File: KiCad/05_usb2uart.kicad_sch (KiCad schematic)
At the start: 16 parts, among them IC501 FT232RL-REEL, J301 USB_C_Receptacle_USB2.0, U301 USBLC6-2SC6

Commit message: First scheme complete
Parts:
- removed D301, D302: LED, LED_SMD:LED_0603_1608Metric, symbol Device:LED
- removed R301, R302: 0R, Resistor_SMD:R_0805_2012Metric, symbol Device:R
- removed R305, R306: 510R, Resistor_SMD:R_0402_1005Metric, symbol Device:R
- added C503: 22uF, Capacitor_SMD:C_0805_2012Metric, symbol Device:C
- added D501, D502, D503: LED, LED_SMD:LED_0603_1608Metric, symbol Device:LED
- added J501, J502: Conn_01x09_Pin, Connector_PinHeader_2.54mm:PinHeader_1x09_P2.54mm_Vertical, symbol Connector:Conn_01x09_Pin
- added J503: Conn_01x06_Pin, Connector_PinHeader_2.54mm:PinHeader_1x06_P2.54mm_Vertical, symbol Connector:Conn_01x06_Pin
- added R503, R504, R505: 510R, Resistor_SMD:R_0402_1005Metric, symbol Device:R
- renumbered C502 to C501, C501 to C502, C304 to C504, C305 to C505, J301 to J504, R303 to R501, R304 to R502, R307 to R506, U301 to U501
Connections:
- net +VCC_USB2UART_FILT: now also D501.2 (A), D502.2 (A), J502.6 (Pin_6)
- net GND: now also C503.2, D503.1 (K), J501.7 (Pin_7), J502.8 (Pin_8), J503.6 (Pin_6)
- net RXD: now also IC501.5 (RXD), J501.5 (Pin_5), J503.2 (Pin_2)
- net RX_LED: now also R504.1
- net TXD: now also IC501.1 (TXD), J501.1 (Pin_1), J503.3 (Pin_3)
- net TX_LED: now also J502.7 (Pin_7), R505.1
- net DCD: now reaches IC501.10 (DCD#)
- net DCD: now also J501.8 (Pin_8), J501.9 (Pin_9)
- net CTS: now reaches IC501.11 (CTS#)
- net CTS: now also J502.4 (Pin_4), J503.5 (Pin_5)
- net SLEEP: now reaches IC501.12 (CBUS4)
- net SLEEP: now also J502.3 (Pin_3)
- net TEN: now reaches IC501.13 (CBUS2)
- net TEN: now also J502.2 (Pin_2)
- net PWREN: now reaches IC501.14 (CBUS3)
- net PWREN: now also J502.1 (Pin_1)
- net +3V3_FTDI: now reaches IC501.17 (3V3OUT)
- net +3V3_FTDI: now also C503.1, J502.5 (Pin_5), R503.2
- net DTR: now reaches IC501.2 (DTR#)
- net DTR: now also J501.2 (Pin_2), J502.9 (Pin_9), J503.1 (Pin_1)
- net RTS: now reaches IC501.3 (RTS#)
- net RTS: now also J501.3 (Pin_3)
- net RI: now reaches IC501.6 (RI#)
- net RI: now also J501.6 (Pin_6)
- net DSR: now reaches IC501.9 (DSR#)
- new net: D501.1 (K), R504.2
- new net: D503.2 (A), R503.1
- new net: D502.1 (K), R505.2
- new net FTDI_VCC: J503.4 (Pin_4)
- new net VCC_FTDI: J501.4 (Pin_4)
- no-connect marks 9 -> 5
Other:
- note added: "Pin headers"
- note added: "Power indication"
- note added: "TX/RX indication"
- moved on the sheet: C501, C502, C504, IC501, J504, R501, R502, U501

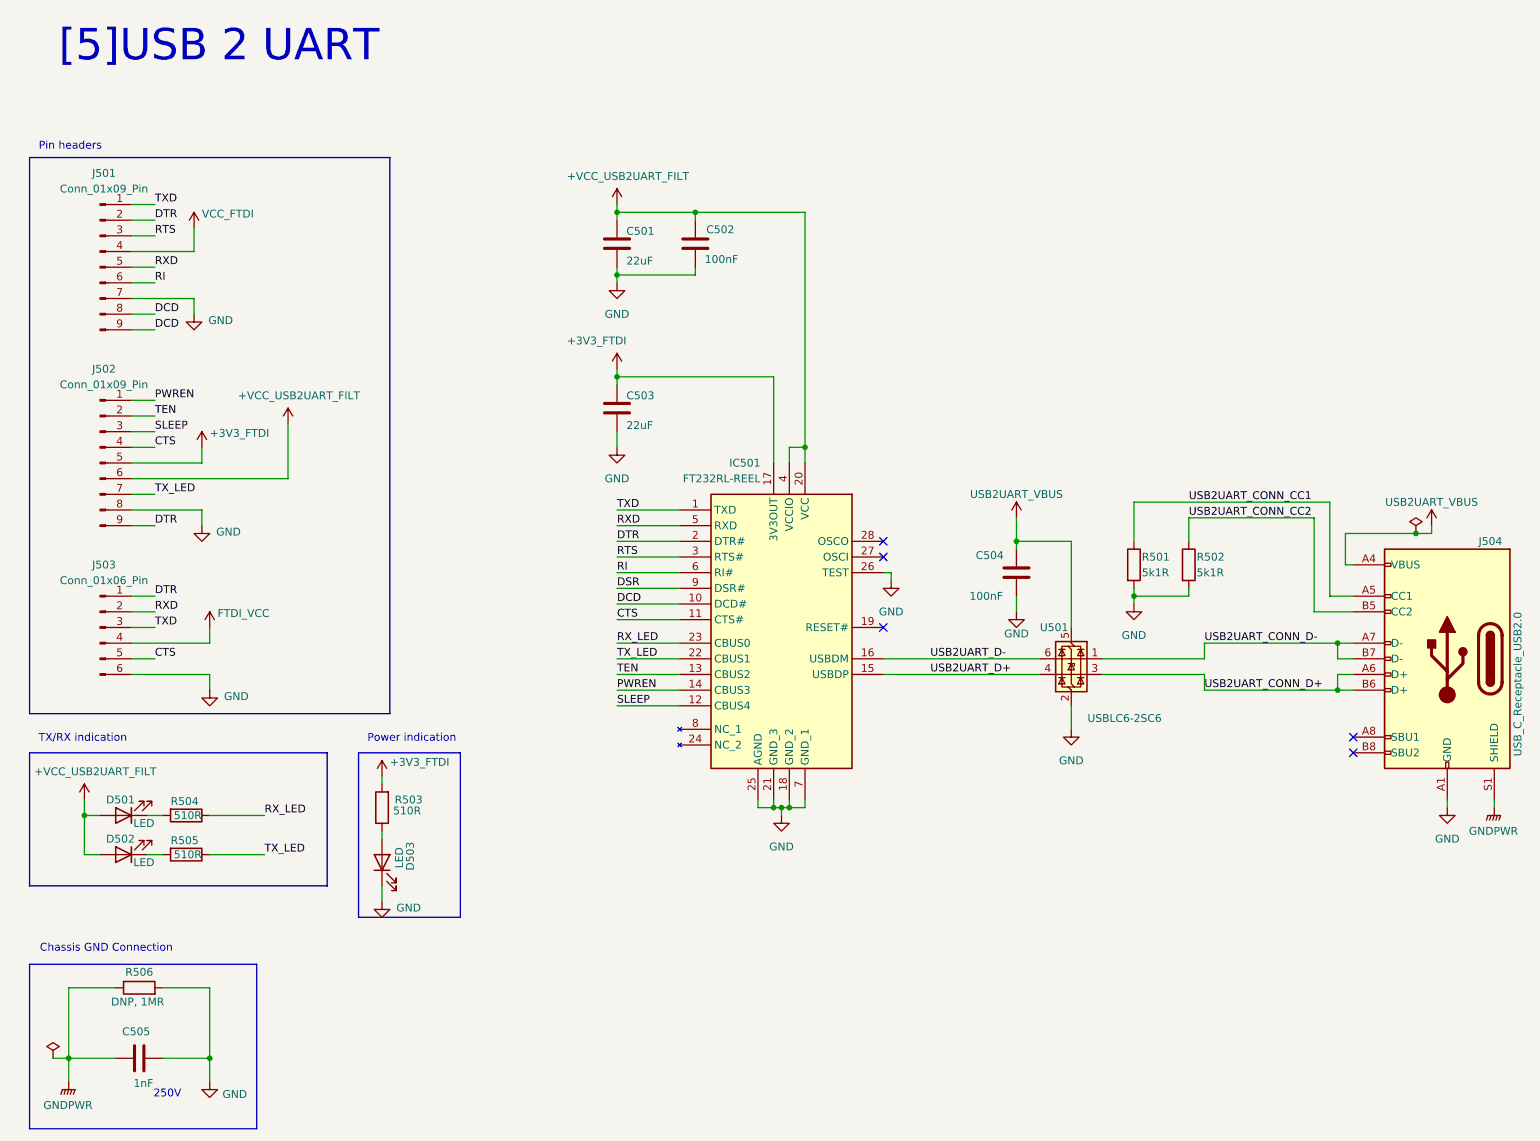
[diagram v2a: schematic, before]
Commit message: ERC fixes
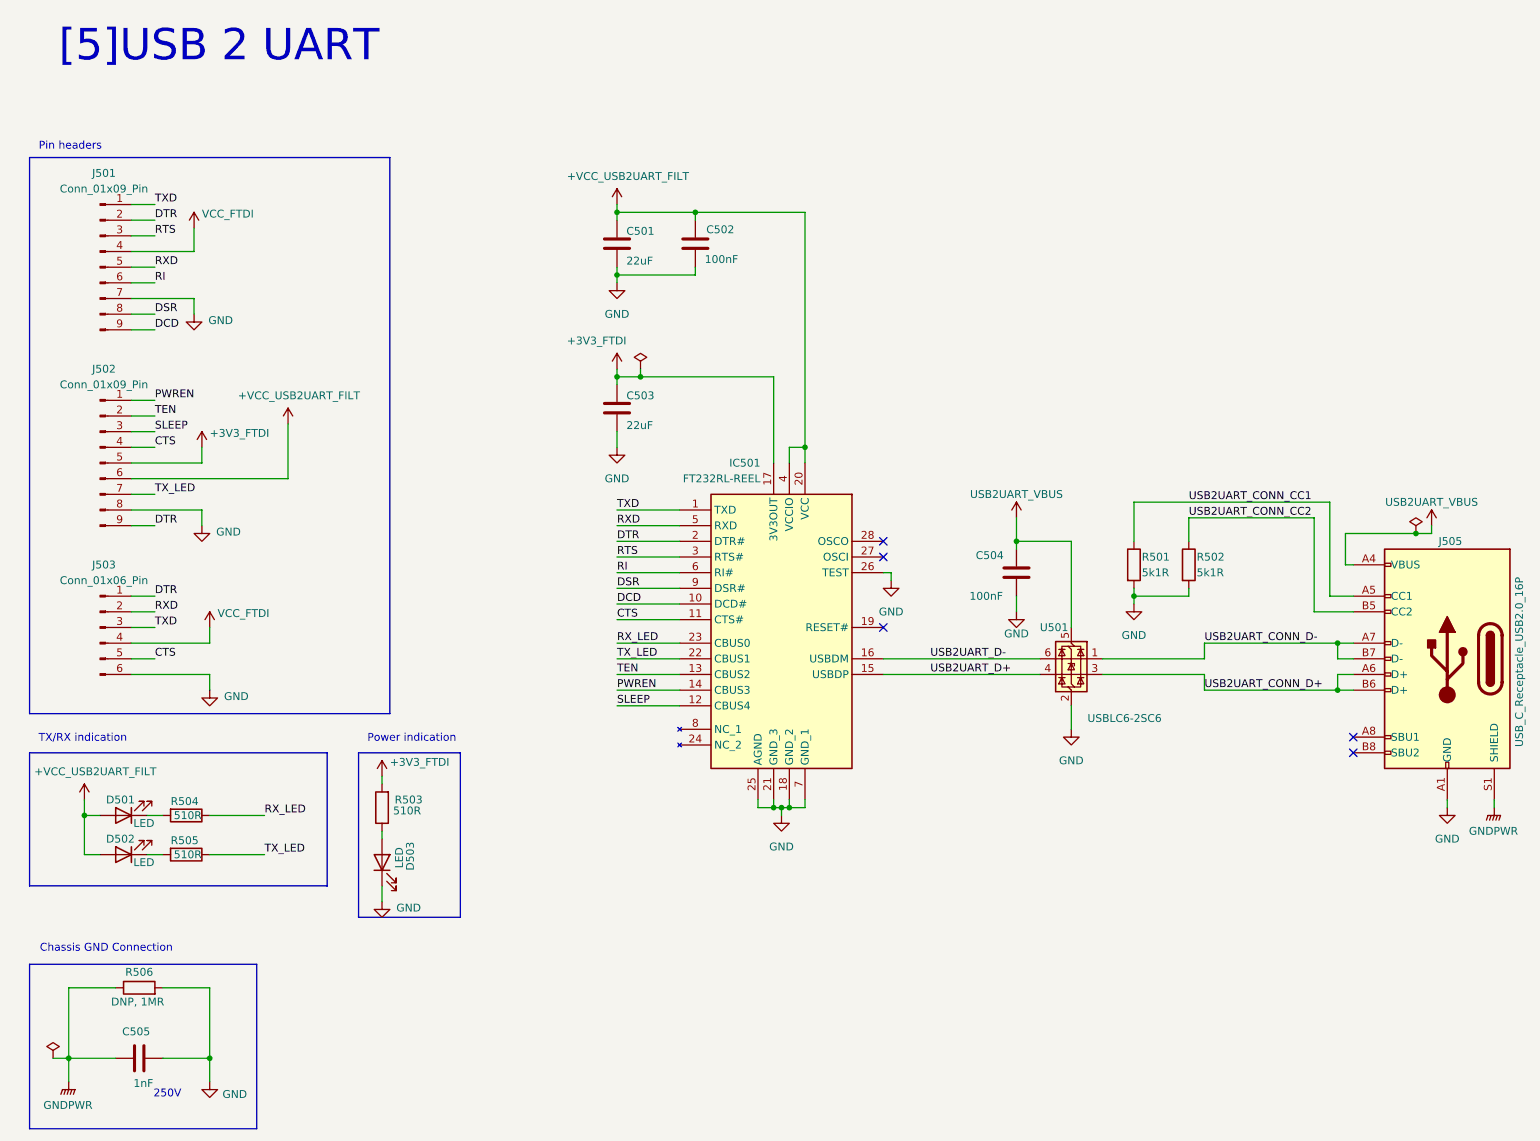
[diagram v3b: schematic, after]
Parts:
- removed J504: USB_C_Receptacle_USB2.0, Connector_USB:USB_C_Receptacle_HRO_TYPE-C-31-M-12, symbol Connector:USB_C_Receptacle_USB2.0
- added J505: USB_C_Receptacle_USB2.0_16P, Connector_USB:USB_C_Receptacle_HRO_TYPE-C-31-M-12, symbol Connector:USB_C_Receptacle_USB2.0_16P
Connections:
- net FTDI_VCC is gone; now on net VCC_FTDI: J503.4 (Pin_4)
- net DCD: no longer J501.8 (Pin_8)
- net DSR: now also J501.8 (Pin_8)
- net GND: now also J505.A1 (GND), J505.A12 (GND), J505.B1 (GND), J505.B12 (GND)
- net GNDPWR: now also J505.S1 (SHIELD)
- net USB2UART_CONN_CC1: now also J505.A5 (CC1)
- net USB2UART_CONN_CC2: now also J505.B5 (CC2)
- net USB2UART_CONN_D+: now also J505.A6 (D+), J505.B6 (D+)
- net USB2UART_CONN_D-: now also J505.A7 (D-), J505.B7 (D-)
- net USB2UART_VBUS: now also J505.A4 (VBUS), J505.A9 (VBUS), J505.B4 (VBUS), J505.B9 (VBUS)

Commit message: basic PCB
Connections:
- net DTR: no longer J502.9 (Pin_9)
- net RX_LED: now also J502.9 (Pin_9)
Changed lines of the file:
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@@
+		)
+	)
+	(label "RX_LED"
+		(at 34.29 97.79 0)
+		(effects
+			(font
+				(size 1.27 1.27)
+			)
+			(justify left bottom)
 		)
 	)
@@
 		)
 	)
-	(label "DTR"
-		(at 34.29 97.79 0)
-		(effects
-			(font
-				(size 1.27 1.27)
-			)
-			(justify left bottom)
-		)
-	)
 	(label "TEN"
 		(at 109.22 121.92 0)
@@
 		(dnp no)
 		(property "Reference" "R503"
-			(at 75.438 142.24 0)
+			(at 74.93 141.986 0)
 			(effects
 				(font
@@
 		(dnp no)
 		(property "Reference" "D503"
-			(at 75.692 151.384 0)
+			(at 75.692 151.384 90)
 			(effects
 				(font
@@
 		)
 		(property "Value" "LED"
-			(at 73.914 151.638 0)
-			(effects
-				(font
+			(at 75.692 153.162 90)
+			(effects
+				(font

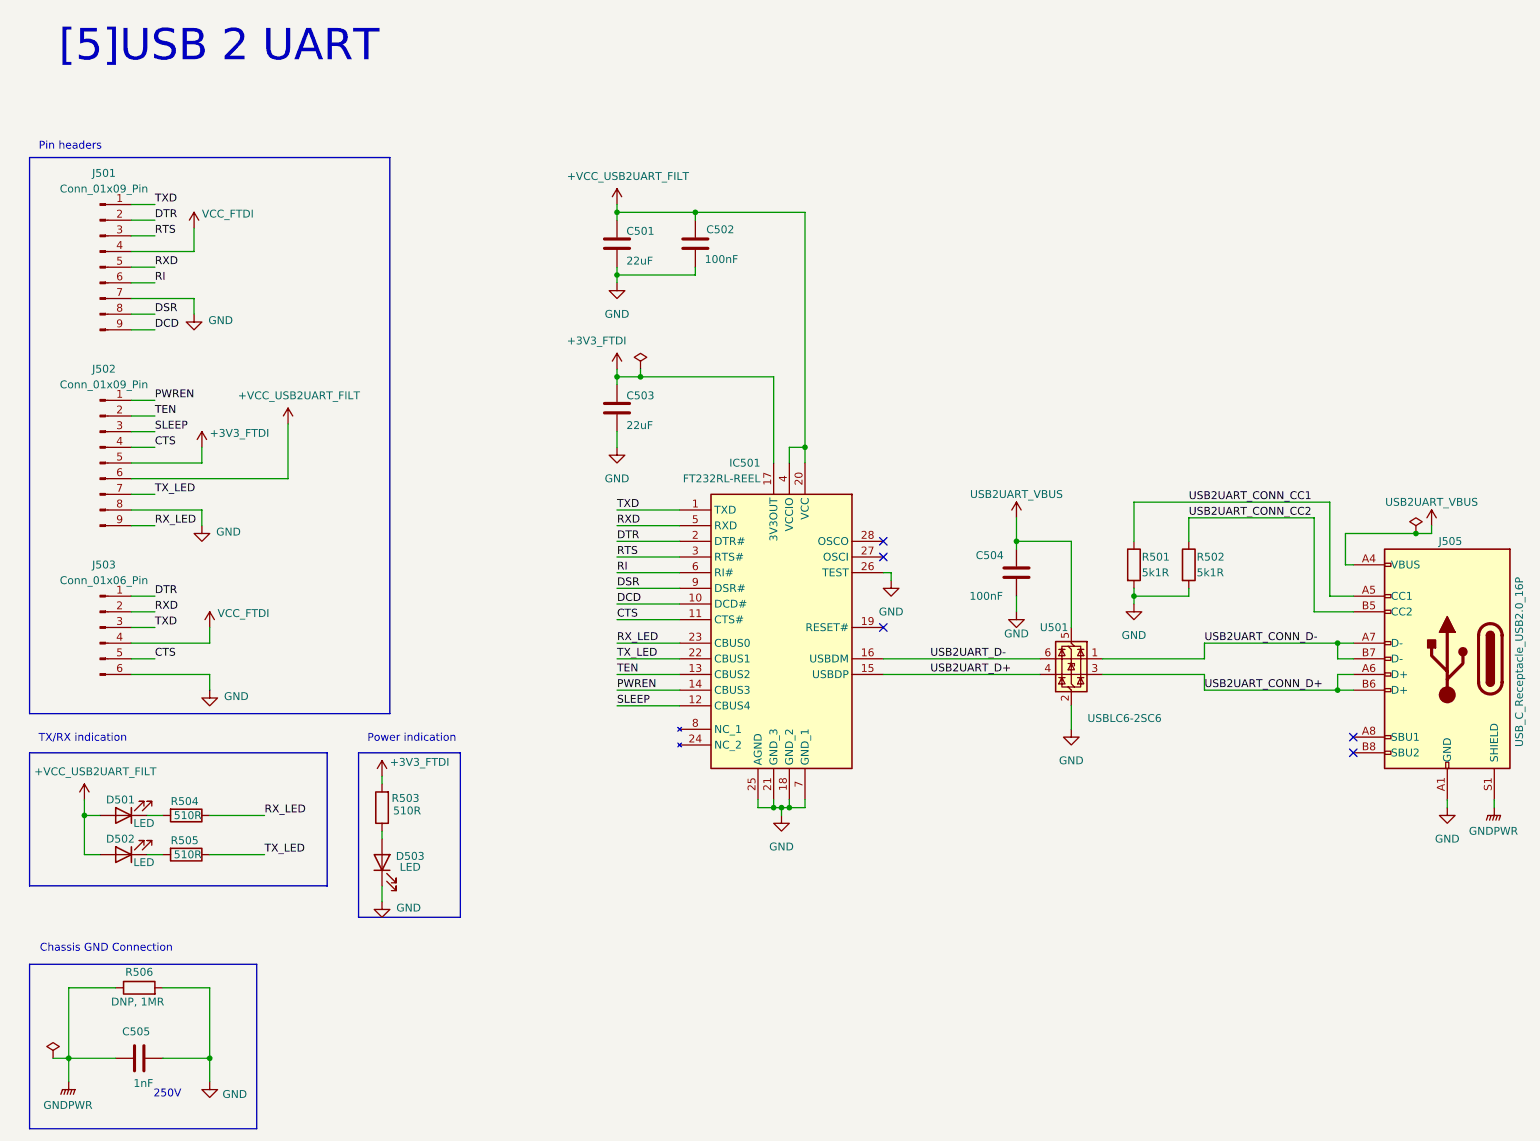
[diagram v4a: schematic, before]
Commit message: Calculated pin headers positions
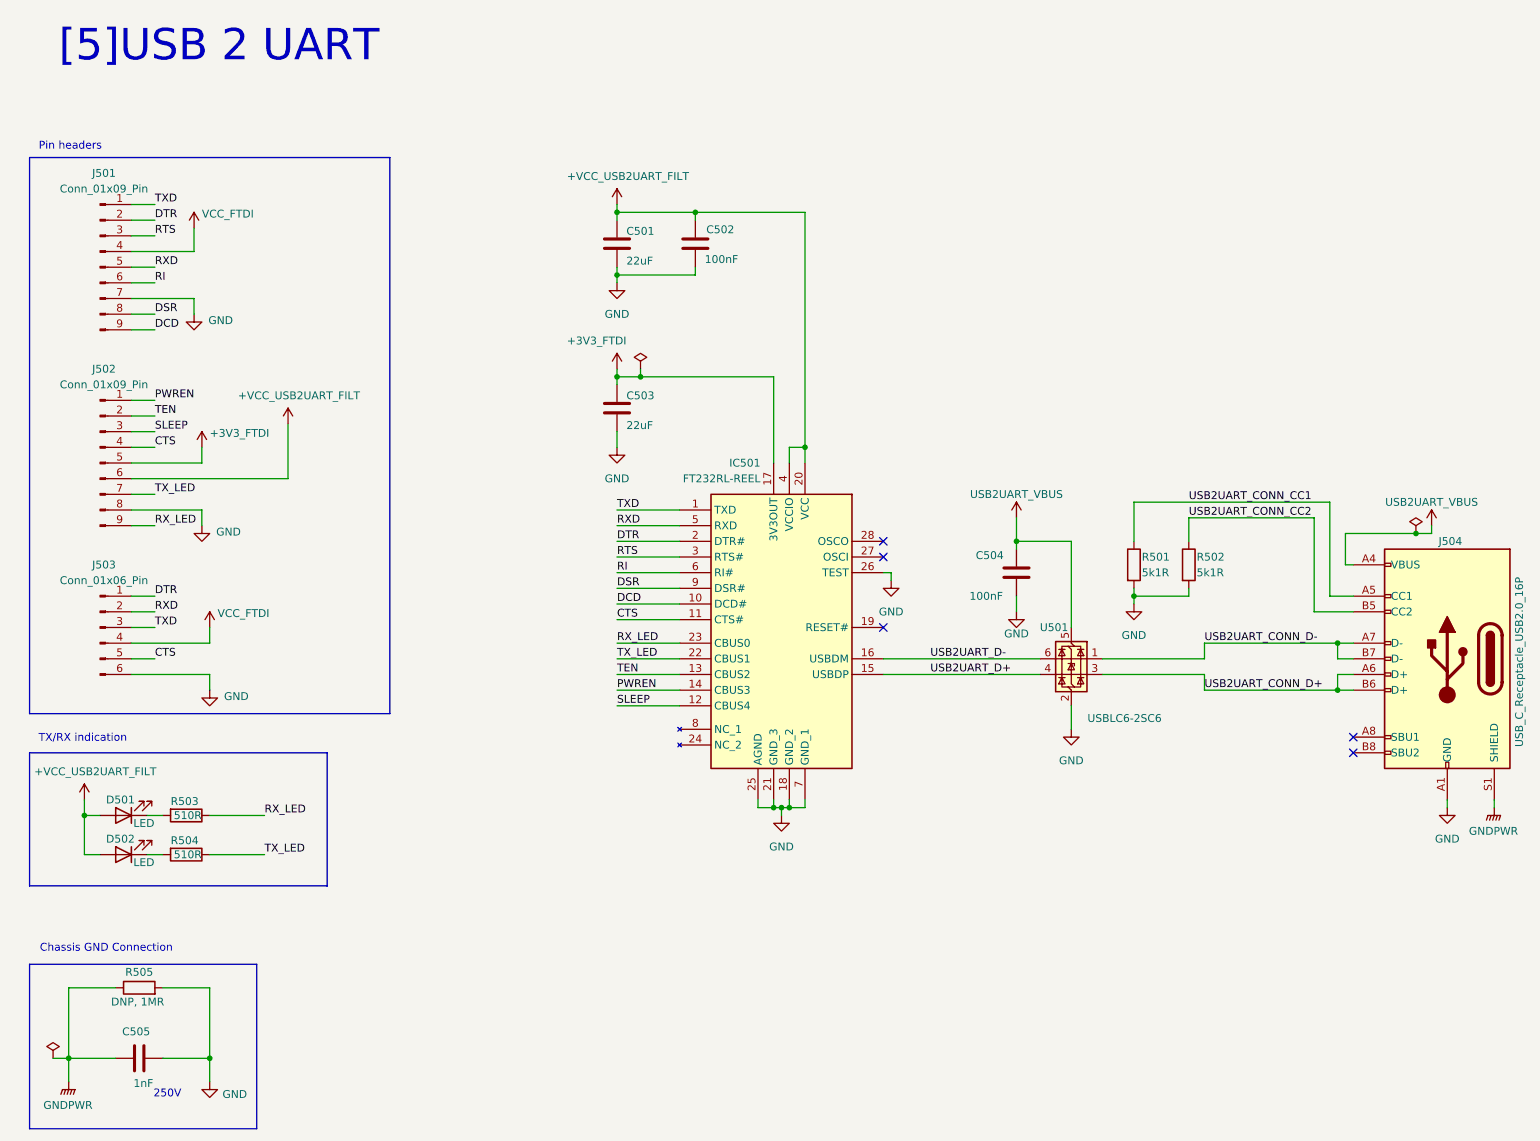
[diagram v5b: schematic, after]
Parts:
- removed D503: LED, LED_SMD:LED_0603_1608Metric, symbol Device:LED
- removed R503: 510R, Resistor_SMD:R_0402_1005Metric, symbol Device:R
- renumbered J505 to J504, R504 to R503, R505 to R504, R506 to R505
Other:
- note removed: "Power indication"

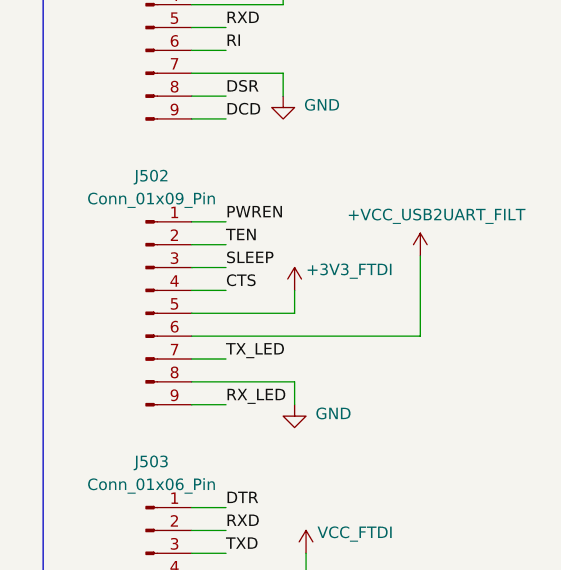
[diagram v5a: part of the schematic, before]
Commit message: Update FTDI pin header
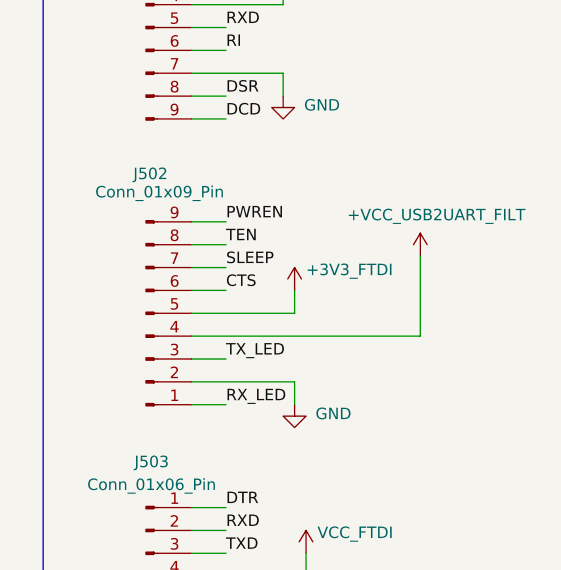
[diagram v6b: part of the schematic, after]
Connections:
- net +VCC_USB2UART_FILT: now also J502.4 (Pin_4); no longer J502.6 (Pin_6)
- net CTS: now also J502.6 (Pin_6); no longer J502.4 (Pin_4)
- net GND: now also J502.2 (Pin_2); no longer J502.8 (Pin_8)
- net PWREN: now also J502.9 (Pin_9); no longer J502.1 (Pin_1)
- net RX_LED: now also J502.1 (Pin_1); no longer J502.9 (Pin_9)
- net SLEEP: now also J502.7 (Pin_7); no longer J502.3 (Pin_3)
- net TEN: now also J502.8 (Pin_8); no longer J502.2 (Pin_2)
- net TX_LED: now also J502.3 (Pin_3); no longer J502.7 (Pin_7)
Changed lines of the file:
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@@
 		(lib_id "Connector:Conn_01x09_Pin")
 		(at 25.4 87.63 0)
+		(mirror x)
 		(unit 1)
 		(exclude_from_sim no)
@@
 		(on_board yes)
 		(dnp no)
-		(fields_autoplaced yes)
 		(property "Reference" "J502"
-			(at 26.035 72.39 0)
+			(at 25.908 72.136 0)
 			(effects
 				(font
@@
 		)
 		(property "Value" "Conn_01x09_Pin"
-			(at 26.035 74.93 0)
+			(at 26.924 74.168 0)
 			(effects
 				(font
